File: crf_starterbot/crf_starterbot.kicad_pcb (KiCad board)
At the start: 2 copper layers, 49 parts, among them J101 Screw_Terminal_01x02, J102 Conn_01x10_Female, J103 Screw_Terminal_01x02, J104 Screw_Terminal_01x02, Q101 Q_NPN_BCE, SW101 SW_SPST, SW102 SW_SPST, SW103 SW_SPST, U101 WeMos_D1_mini, U102 HC-SR04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

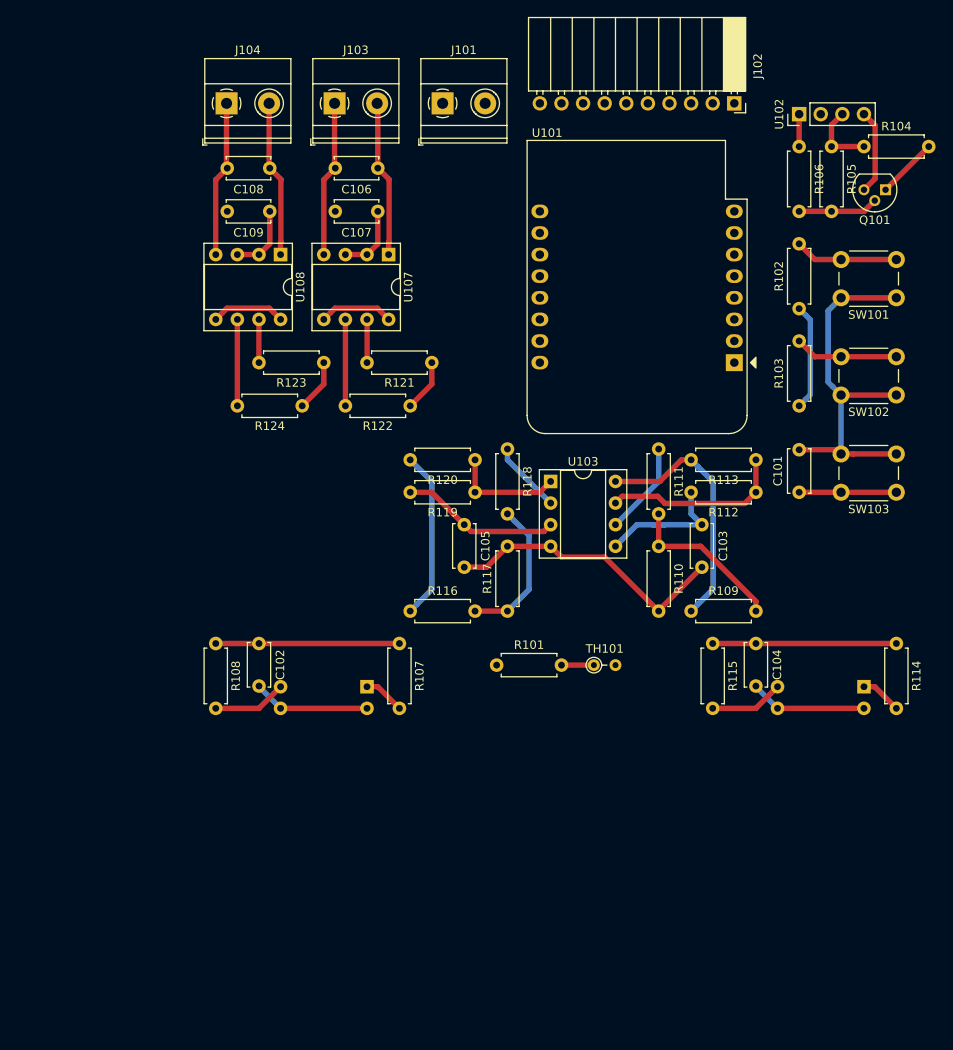
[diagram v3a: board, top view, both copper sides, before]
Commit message: Completed routing of all components except thermistor and phototransistors, need to discuss those with robert
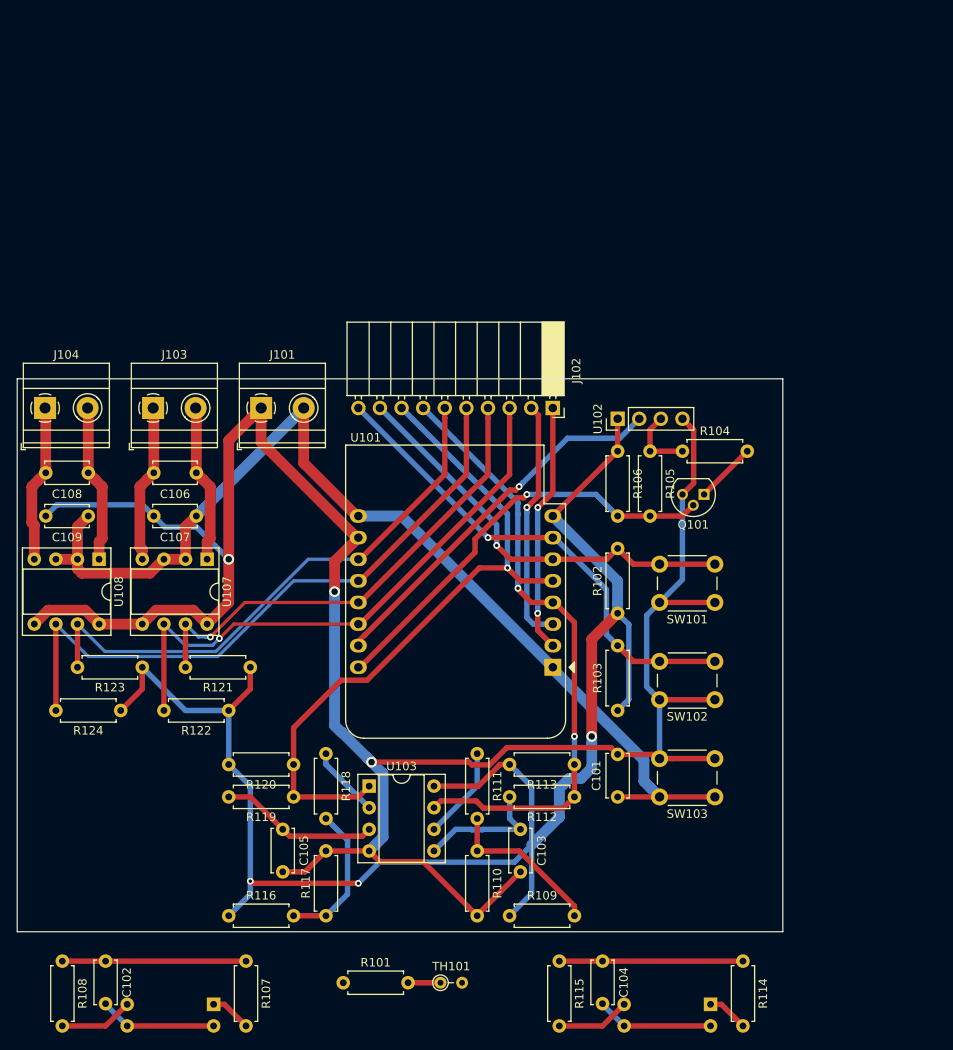
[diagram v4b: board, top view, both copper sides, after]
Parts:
- moved Q101 41.7 mm to (110.7, 53.6)
- moved R104 41.7 mm to (108.2, 48.5)
- moved R105 41.7 mm to (104.4, 48.5)
- moved R106 41.7 mm to (100.6, 48.5)
- moved R110 41.7 mm to (84.1, 95.5)
- moved SW102 41.7 mm to (112.0, 77.7)
- moved C103 41.7 mm to (89.2, 93.0)
- moved C105 41.7 mm to (61.2, 93.0)
- moved C106 41.7 mm to (51.1, 51.1)
- moved C107 41.7 mm to (51.1, 56.1)
- moved C108 41.7 mm to (38.4, 51.1)
- moved C109 41.7 mm to (38.4, 56.1)
- moved J101 41.7 mm to (58.7, 43.4)
- moved J102 41.7 mm to (93.0, 43.4)
- moved J103 41.7 mm to (46.0, 43.4)
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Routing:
- net GND: track 133.7 -> 298.0 mm, vias 0 -> 3
- net +3V3: track 121.5 -> 233.0 mm, vias 0 -> 3
- net +BATT: track 27.7 -> 124.0 mm
- net RIGHT_ENC: track 13.2 -> 80.4 mm, vias 0 -> 1
- net RIGHTA: track 10.2 -> 76.7 mm
- net RIGHTB: track 5.08 -> 66.0 mm
- net LEFTA: track 10.2 -> 68.0 mm, vias 0 -> 1
- net LEFTB: track 5.08 -> 57.0 mm, vias 0 -> 1
- net LEFT_ENC: track 21.5 -> 72.4 mm, vias 0 -> 2
- net RIGHT_SW: track 12.2 -> 57.3 mm, vias 0 -> 1
- net TRIG: track 0.00 -> 44.4 mm, vias 0 -> 1
- net ECHO: track 9.42 -> 50.3 mm, vias 0 -> 1
- net LEFT_SW: track 12.2 -> 49.5 mm, vias 0 -> 1
- net TEMP: track 3.81 -> 33.2 mm, vias 0 -> 2
- net Net-(J102-Pad2): track 0.00 -> 28.9 mm, vias 0 -> 1
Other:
- board outline added: 90 x 65 mm
